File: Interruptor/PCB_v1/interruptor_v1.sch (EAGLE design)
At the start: 0 parts

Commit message: Schematic of ZCD and MIDI
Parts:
- added C1: 10uF, rcl:C-EUC0805
- added C2, C4: 100nF, rcl:C-EUC0805
- added C3: 10nF, rcl:C-EUC0805
- added C5: ??, rcl:C-EUC0805
- added D1: (no value), diode:DIODE-DO214AA
- added IC1: ICM7555, maxim:ICM7555
- added P1: (no value), audio:RN-114
- added R1: PC16D, piher:PC16D
- added R10, R11, R6, R7, R9: 2.2k, resistor:R-EU_M0805
- added R2, R3, R4: (no value), resistor:R-EU_M0805
- added R5: 220, resistor:R-EU_M0805
- added R8: 22k, resistor:R-EU_M0805
- added S1: 50-3POLE30, switch:50-3POLE30
- added SV1: I2C, con-lstb:MA04-1
- added T1, T2: (no value), zetex:NMOSSOT23
- added U$1: MCP6001RT-E/OT, MCP6001RT-E_OT:MCP6001RT-E/OT
- added U1: (no value), esp8266modules:ESP12SMD
- added U2: TCLD1000, TCLD1000:TCLD1000
- added X1: MAB5SH, con-hirschmann:MAB5SH
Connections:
- new net 3V3: IC1.RESET, IC1.V+, R1.1E, R1.1S, R1.2E, R10.1, R2.1, R3.1, R4.2, SV1.1, U$1.VDD, U1.CH_PD, U1.VCC
- new net ESP_TRIG_OUT: S1.B1, S1.B2, U1.GPIO2
- new net GND: C2.1, C4.1, C5.1, IC1.GND, R1.2A, SV1.4, T2.S, U$1.VSS, U1.GND, U1.GPIO15, U2.E1
- new net N$1: R4.1, U2.CO1
- new net N$10: C3.2, R7.1, R8.2, U$1.VIN-
- new net N$11: IC1.TRIG, R10.2, T2.D
- new net N$12: C3.1, R8.1, R9.2, U$1.VOUT
- new net N$13: C4.2, IC1.CV
- new net N$14: R9.1, T2.G
- new net N$16: C5.2, IC1.DISCH, IC1.TRSH, R1.1A
- new net N$18: IC1.OUT, S1.B3
- new net N$2: R5.2, X1.4
- new net N$20: R11.1, S1.B
- new net N$21: R11.2, T1.G
- new net N$3: D1.C, R5.1, U2.A1
- new net N$4: D1.A, U2.C1, X1.5
- new net N$5: R1.2S, U1.ADC
- new net N$6: C1.1, P1.TIP
- new net N$7: C2.2, P1.SLEEVE, R7.2
- new net N$8: C1.2, R6.2
- new net N$9: R6.1, U$1.VIN+
- new net PGM: U1.GPIO0
- new net RX: U1.RX
- new net SCL: R2.2, SV1.2, U1.GPIO4
- new net SDA: R3.2, SV1.3, U1.GPIO5

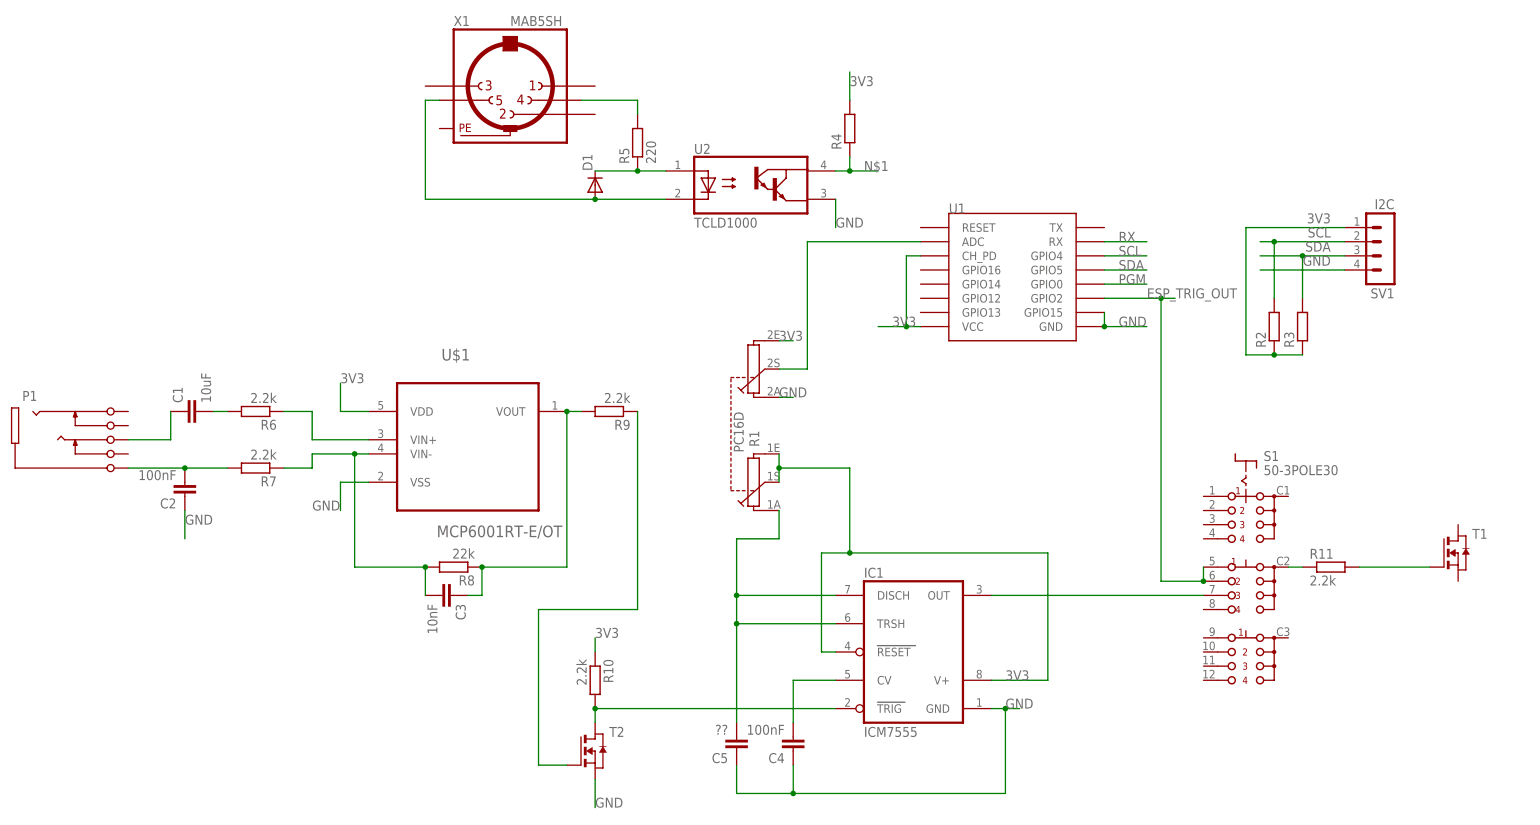
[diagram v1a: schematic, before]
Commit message: Finished with 1/4
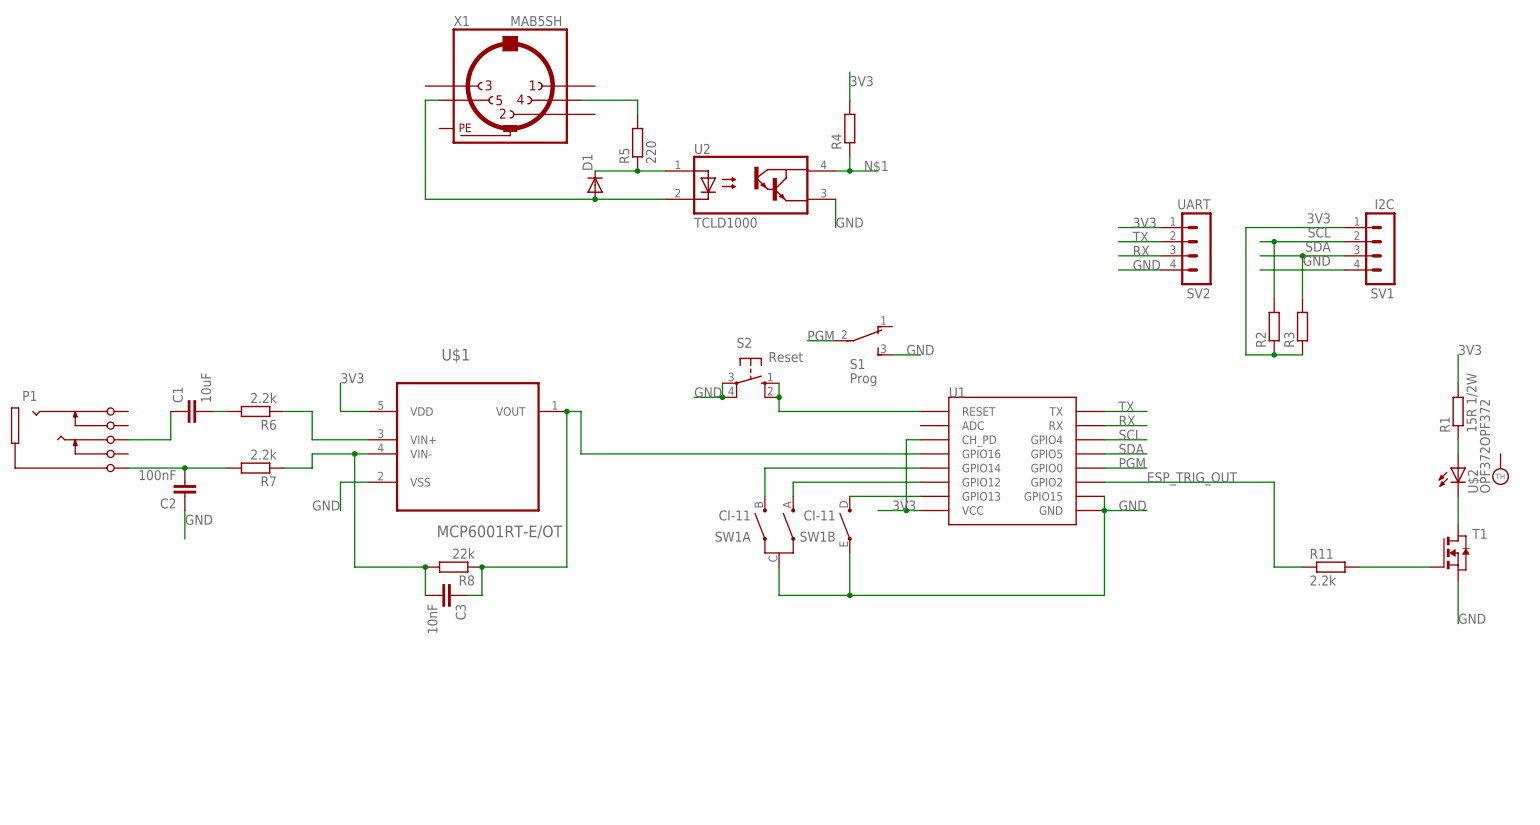
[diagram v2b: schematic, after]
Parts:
- removed C4: 100nF, rcl:C-EUC0805
- removed C5: ??, rcl:C-EUC0805
- removed IC1: ICM7555, maxim:ICM7555
- removed R10, R9: 2.2k, resistor:R-EU_M0805
- removed T2: (no value), zetex:NMOSSOT23
- added S2: Reset, switch-omron:10-XX
- added SV2: UART, con-lstb:MA04-1
- added SW1: CI-11, piher:CI-11
- added U$2: OPF372OPF372, fibre:OPF372OPF372
- R1: value PC16D -> 15R 1/2W; device piher:PC16D -> resistor:R-EU_M0805
- S1: value 50-3POLE30 -> Prog; device switch:50-3POLE30 -> switch:TL36YO
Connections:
- removed net N$18: IC1.OUT, S1.B3
- removed net N$20: R11.1, S1.B
- new net N$15: S2.S, S2.S1, U1.RESET
- new net TX: SV2.2, U1.TX
- net 3V3: now also R1.2, SV2.1; no longer IC1.RESET, IC1.V+, R1.1E, R1.1S, R1.2E, R10.1
- net ESP_TRIG_OUT: now also R11.1; no longer S1.B1, S1.B2
- net GND: now also S1.S, S2.P, S2.P1, SV2.4, SW1A.C, SW1B.E, T1.S; no longer C4.1, C5.1, IC1.GND, R1.2A, T2.S
- net N$11: now also SW1A.A, U1.GPIO12; no longer IC1.TRIG, R10.2, T2.D
- net N$12: now also U1.GPIO16; no longer R9.2
- net N$13: now also SW1A.B, U1.GPIO14; no longer C4.2, IC1.CV
- net N$14: now also T1.D, U$2.C; no longer R9.1, T2.G
- net N$16: now also R1.1, U$2.A; no longer C5.2, IC1.DISCH, IC1.TRSH, R1.1A
- net N$5: now also SW1B.D, U1.GPIO13; no longer R1.2S, U1.ADC
- net PGM: now also S1.P
- net RX: now also SV2.3
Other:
- moved on the sheet: U1

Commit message: No DRC, now to route
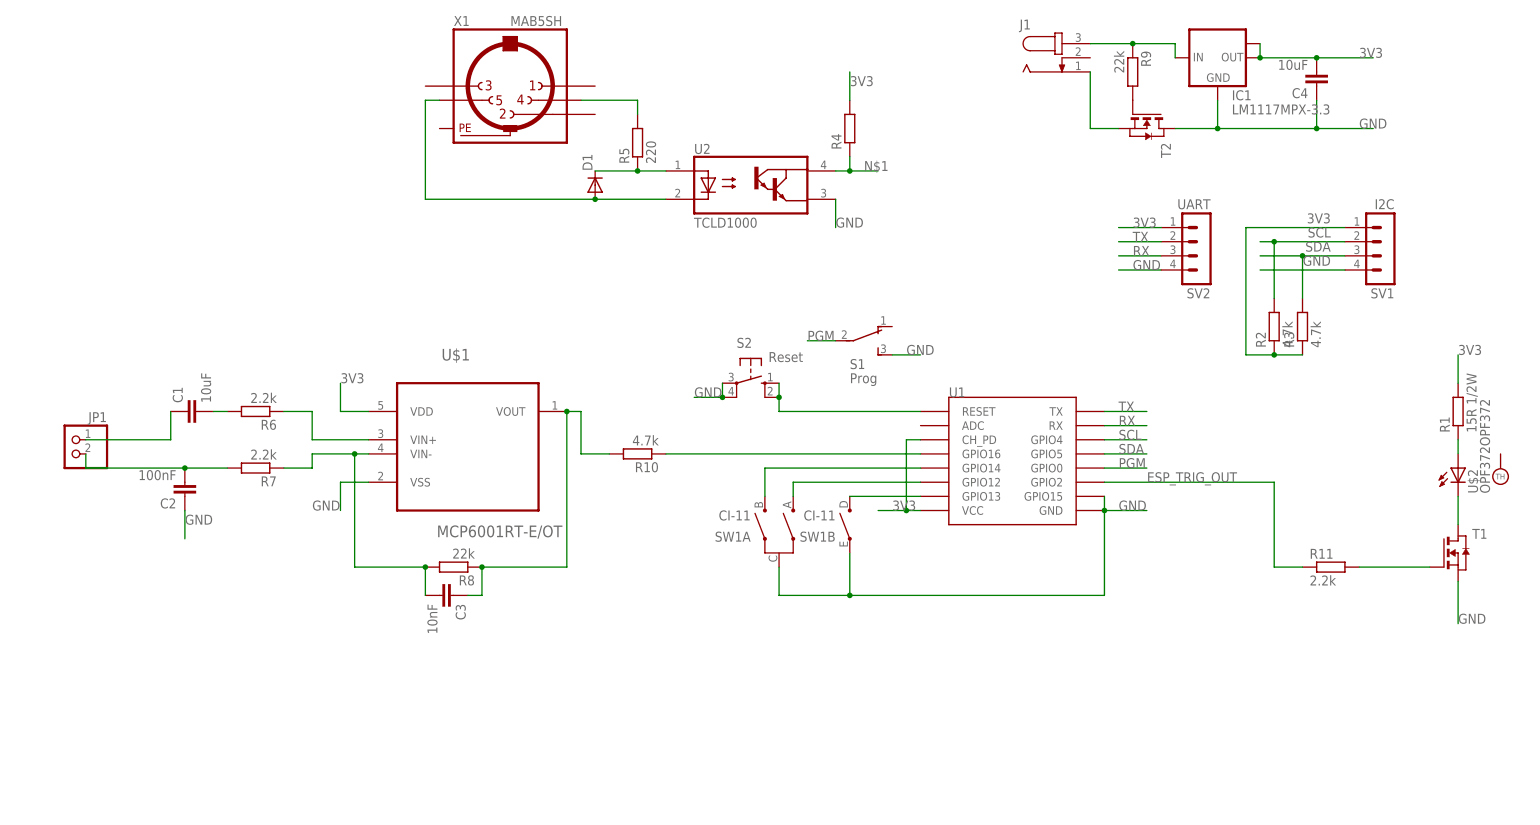
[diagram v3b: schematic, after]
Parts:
- removed P1: (no value), audio:RN-114
- added C4: 10uF, rcl:C-EUC0805
- added IC1: LM1117MPX-3.3, lm1117:LM1117MPX-3.3
- added J1: (no value), con-jack:JACK-PLUG0
- added JP1: (no value), pinhead:PINHD-1X2
- added R10: 4.7k, resistor:R-EU_M0805
- added R9: 22k, resistor:R-EU_M0805
- added T2: (no value), zetex:NMOSSOT23
- R2, R3: value (none) -> 4.7k
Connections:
- new net N$17: J1.1, T2.S
- new net N$18: IC1.IN, J1.3, R9.1
- new net N$19: R9.2, T2.G
- new net N$20: R10.1, U1.GPIO16
- net 3V3: now also C4.2, IC1.OUT, IC1.OUT1
- net GND: now also C4.1, IC1.GND, T2.D
- net N$12: now also R10.2; no longer U1.GPIO16
- net N$6: now also JP1.1; no longer P1.TIP
- net N$7: now also JP1.2; no longer P1.SLEEVE
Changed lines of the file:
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@@
 <layer number="98" name="Guide" color="6" fill="1" visible="yes" active="yes"/>
 <layer number="99" name="SpiceOrder" color="5" fill="1" visible="yes" active="yes"/>
+<layer number="250" name="Descript" color="3" fill="1" visible="no" active="no"/>
+<layer number="251" name="SMDround" color="12" fill="11" visible="no" active="no"/>
 </layers>
 <schematic xreflabel="%F%N/%S.%C%R" xrefpart="/%S.%C%R">
@@
 <part name="SV1" library="con-lstb" deviceset="MA04-1" device="" value="I2C"/>
 <part name="T1" library="zetex" deviceset="NMOSSOT23" device=""/>
-<part name="R2" library="resistor" deviceset="R-EU_" device="M0805"/>
-<part name="R3" library="resistor" deviceset="R-EU_" device="M0805"/>
+<part name="R2" library="resistor" deviceset="R-EU_" device="M0805" value="4.7k"/>
+<part name="R3" library="resistor" deviceset="R-EU_" device="M0805" value="4.7k"/>
 <part name="R4" library="resistor" deviceset="R-EU_" device="M0805"/>
 <part name="R5" library="resistor" deviceset="R-EU_" device="M0805" value="220"/>
 <part name="D1" library="diode" deviceset="DIODE-" device="DO214AA"/>
-<part name="P1" library="audio" deviceset="RN-114" device=""/>
 <part name="C1" library="rcl" deviceset="C-EU" device="C0805" value="10uF"/>
 <part name="R6" library="resistor" deviceset="R-EU_" device="M0805" value="2.2k"/>
@@
 <part name="S2" library="switch-omron" deviceset="10-XX" device="" value="Reset"/>
 <part name="SV2" library="con-lstb" deviceset="MA04-1" device="" value="UART"/>
+<part name="JP1" library="pinhead" deviceset="PINHD-1X2" device=""/>
+<part name="J1" library="con-jack" deviceset="JACK-PLUG" device="0"/>
+<part name="C4" library="rcl" deviceset="C-EU" device="C0805" value="10uF"/>
+<part name="IC1" library="lm1117" deviceset="LM1117MPX-*" device="" technology="3.3"/>
+<part name="T2" library="zetex" deviceset="NMOSSOT23" device=""/>
+<part name="R9" library="resistor" deviceset="R-EU_" device="M0805" value="22k"/>
+<part name="R10" library="resistor" deviceset="R-EU_" device="M0805" value="4.7k"/>
 </parts>
 <sheets>
@@
 <instance part="R5" gate="G$1" x="58.42" y="124.46" rot="R90"/>
 <instance part="D1" gate="G$1" x="50.8" y="116.84" rot="R90"/>
-<instance part="P1" gate="G$1" x="-53.34" y="73.66"/>
 <instance part="C1" gate="G$1" x="-22.86" y="76.2" rot="R90"/>
 <instance part="R6" gate="G$1" x="-10.16" y="76.2" rot="R180"/>
@@
 <instance part="S2" gate="1" x="78.74" y="81.28" rot="R270"/>
 <instance part="SV2" gate="1" x="160.02" y="104.14" rot="R180"/>
+<instance part="JP1" gate="G$1" x="-43.18" y="68.58" rot="MR0"/>
+<instance part="J1" gate="G$1" x="134.62" y="139.7"/>
+<instance part="C4" gate="G$1" x="180.34" y="134.62" rot="R180"/>
+<instance part="IC1" gate="G$1" x="162.56" y="139.7"/>
+<instance part="T2" gate="A" x="149.86" y="127" rot="R270"/>
+<instance part="R9" gate="G$1" x="147.32" y="137.16" rot="R270"/>
+<instance part="R10" gate="G$1" x="58.42" y="68.58" rot="R180"/>
 </instances>
 <busses>
@@
 <wire x1="152.4" y1="109.22" x2="144.78" y2="109.22" width="0.1524" layer="91"/>
 <label x="147.32" y="109.22" size="1.778" layer="95"/>
+</segment>
+<segment>
+<pinref part="IC1" gate="G$1" pin="OUT1"/>
+<pinref part="IC1" gate="G$1" pin="OUT"/>
+<wire x1="170.18" y1="142.24" x2="170.18" y2="139.7" width="0.1524" layer="91"/>
+<pinref part="C4" gate="G$1" pin="2"/>
+<wire x1="180.34" y1="139.7" x2="170.18" y2="139.7" width="0.1524" layer="91"/>
+<junction x="170.18" y="139.7"/>
+<wire x1="180.34" y1="139.7" x2="190.5" y2="139.7" width="0.1524" layer="91"/>
+<junction x="180.34" y="139.7"/>
+<label x="187.96" y="139.7" size="1.778" layer="95"/>
 </segment>
 </net>
@@
 <label x="147.32" y="101.6" size="1.778" layer="95"/>
 </segment>
+<segment>
+<pinref part="IC1" gate="G$1" pin="GND"/>
+<wire x1="162.56" y1="127" x2="162.56" y2="132.08" width="0.1524" layer="91"/>
+<pinref part="C4" gate="G$1" pin="1"/>
+<wire x1="180.34" y1="132.08" x2="180.34" y2="127" width="0.1524" layer="91"/>
+<wire x1="180.34" y1="127" x2="162.56" y2="127" width="0.1524" layer="91"/>
+<wire x1="180.34" y1="127" x2="190.5" y2="127" width="0.1524" layer="91"/>
+<junction x="180.34" y="127"/>
+<label x="187.96" y="127" size="1.778" layer="95"/>
+<pinref part="T2" gate="A" pin="D"/>
+<wire x1="162.56" y1="127" x2="154.94" y2="127" width="0.1524" layer="91"/>
+<junction x="162.56" y="127"/>
+</segment>
 </net>
 <net name="N$1" class="0">
@@
 <net name="N$6" class="0">
 <segment>
-<pinref part="P1" gate="G$1" pin="TIP"/>
 <pinref part="C1" gate="G$1" pin="1"/>
-<wire x1="-33.02" y1="71.12" x2="-25.4" y2="71.12" width="0.1524" layer="91"/>
 <wire x1="-25.4" y1="71.12" x2="-25.4" y2="76.2" width="0.1524" layer="91"/>
+<pinref part="JP1" gate="G$1" pin="1"/>
+<wire x1="-25.4" y1="71.12" x2="-40.64" y2="71.12" width="0.1524" layer="91"/>
 </segment>
 </net>
 <net name="N$7" class="0">
 <segment>
-<pinref part="P1" gate="G$1" pin="SLEEVE"/>
 <pinref part="R7" gate="G$1" pin="2"/>
-<wire x1="-33.02" y1="66.04" x2="-22.86" y2="66.04" width="0.1524" layer="91"/>
+<wire x1="-40.64" y1="66.04" x2="-22.86" y2="66.04" width="0.1524" layer="91"/>
 <pinref part="C2" gate="G$1" pin="2"/>
 <wire x1="-22.86" y1="66.04" x2="-15.24" y2="66.04" width="0.1524" layer="91"/>
 <junction x="-22.86" y="66.04"/>
+<pinref part="JP1" gate="G$1" pin="2"/>
+<wire x1="-40.64" y1="66.04" x2="-40.64" y2="68.58" width="0.1524" layer="91"/>
 </segment>
 </net>
@@
 <wire x1="45.72" y1="76.2" x2="48.26" y2="76.2" width="0.1524" layer="91"/>
 <junction x="45.72" y="76.2"/>
-<pinref part="U1" gate="G$1" pin="GPIO16"/>
-<wire x1="109.22" y1="68.58" x2="48.26" y2="68.58" width="0.1524" layer="91"/>
 <wire x1="48.26" y1="68.58" x2="48.26" y2="76.2" width="0.1524" layer="91"/>
+<pinref part="R10" gate="G$1" pin="2"/>
+<wire x1="48.26" y1="68.58" x2="53.34" y2="68.58" width="0.1524" layer="91"/>
 </segment>
 </net>
@@
 </segment>
 </net>
+<net name="N$17" class="0">
+<segment>
+<pinref part="J1" gate="G$1" pin="1"/>
+<wire x1="139.7" y1="127" x2="139.7" y2="137.16" width="0.1524" layer="91"/>
+<pinref part="T2" gate="A" pin="S"/>
+<wire x1="139.7" y1="127" x2="144.78" y2="127" width="0.1524" layer="91"/>
+</segment>
+</net>
+<net name="N$19" class="0">
+<segment>
+<pinref part="T2" gate="A" pin="G"/>
+<pinref part="R9" gate="G$1" pin="2"/>
+</segment>
+</net>
+<net name="N$18" class="0">
+<segment>
+<pinref part="J1" gate="G$1" pin="3"/>
+<pinref part="R9" gate="G$1" pin="1"/>
+<wire x1="139.7" y1="142.24" x2="147.32" y2="142.24" width="0.1524" layer="91"/>
+<pinref part="IC1" gate="G$1" pin="IN"/>
+<wire x1="147.32" y1="142.24" x2="154.94" y2="142.24" width="0.1524" layer="91"/>
+<wire x1="154.94" y1="142.24" x2="154.94" y2="139.7" width="0.1524" layer="91"/>
+<junction x="147.32" y="142.24"/>
+</segment>
+</net>
+<net name="N$20" class="0">
+<segment>
+<pinref part="R10" gate="G$1" pin="1"/>
+<pinref part="U1" gate="G$1" pin="GPIO16"/>
+<wire x1="63.5" y1="68.58" x2="109.22" y2="68.58" width="0.1524" layer="91"/>
+</segment>
+</net>

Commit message: No DRC errors other than drill sizes, routed
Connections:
- net GND: now also U$2.TH
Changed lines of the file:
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@@
 <segment>
 <pinref part="T1" gate="A" pin="S"/>
-<wire x1="205.74" y1="45.72" x2="205.74" y2="38.1" width="0.1524" layer="91"/>
+<wire x1="205.74" y1="45.72" x2="205.74" y2="43.18" width="0.1524" layer="91"/>
 <label x="205.74" y="38.1" size="1.778" layer="95"/>
+<pinref part="U$2" gate="G$1" pin="TH"/>
+<wire x1="205.74" y1="43.18" x2="205.74" y2="38.1" width="0.1524" layer="91"/>
+<wire x1="213.36" y1="68.58" x2="218.44" y2="68.58" width="0.1524" layer="91"/>
+<wire x1="218.44" y1="68.58" x2="218.44" y2="43.18" width="0.1524" layer="91"/>
+<wire x1="218.44" y1="43.18" x2="205.74" y2="43.18" width="0.1524" layer="91"/>
+<junction x="205.74" y="43.18"/>
 </segment>
 <segment>
